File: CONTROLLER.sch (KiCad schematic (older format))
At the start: 75 parts, among them J23 Conn_02x03_Odd_Even, J24 ICSP, J25 Raspberry_Pi_2_3, Q13 DTC124E, Q14 DTC124E, Q15 DTC124E, Q16 DTC124E, Q17 DTC124E, Q18 BCX53, U11 CD4052B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

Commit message: RC2
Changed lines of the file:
@@
 U 1 1 5D6B516E
 P 9800 1875
-F 0 "C76" V 10025 1775 50  0000 L CNN
+F 0 "C76" V 10025 1800 50  0000 L CNN
 F 1 "100n" V 9950 1775 50  0000 L CNN
 F 2 "Capacitor_SMD:C_0805_2012Metric_Pad1.15x1.40mm_HandSolder" H 9838 1725 50  0001 C CNN
@@
 U 1 1 5F3CCF67
 P 13950 3925
-F 0 "C79" V 14100 3825 50  0000 L CNN
+F 0 "C79" V 14100 3850 50  0000 L CNN
 F 1 "100n" V 14175 3825 50  0000 L CNN
 F 2 "Capacitor_SMD:C_0805_2012Metric_Pad1.15x1.40mm_HandSolder" H 13988 3775 50  0001 C CNN
@@
 U 1 1 5DC83D54
 P 14200 7225
-F 0 "C81" V 14425 7175 50  0000 L CNN
+F 0 "C81" V 14425 7150 50  0000 L CNN
 F 1 "100n" V 14350 7125 50  0000 L CNN
 F 2 "Capacitor_SMD:C_0805_2012Metric_Pad1.15x1.40mm_HandSolder" H 14238 7075 50  0001 C CNN
@@
 U 1 1 5DC9523F
 P 14800 7725
-F 0 "C82" V 14650 7625 50  0000 L CNN
+F 0 "C82" V 14650 7650 50  0000 L CNN
 F 1 "100n" V 14575 7625 50  0000 L CNN
 F 2 "Capacitor_SMD:C_0805_2012Metric_Pad1.15x1.40mm_HandSolder" H 14838 7575 50  0001 C CNN
@@
 U 1 1 5F2AD05C
 P 3475 1000
-F 0 "C71" V 3250 950 50  0000 L CNN
+F 0 "C71" V 3250 925 50  0000 L CNN
 F 1 "100n" V 3325 900 50  0000 L CNN
 F 2 "Capacitor_SMD:C_0805_2012Metric_Pad1.15x1.40mm_HandSolder" H 3513 850 50  0001 C CNN
@@
 U 1 1 5F3D5069
 P 4475 1000
-F 0 "C72" V 4250 950 50  0000 L CNN
+F 0 "C72" V 4250 925 50  0000 L CNN
 F 1 "100n" V 4325 900 50  0000 L CNN
 F 2 "Capacitor_SMD:C_0805_2012Metric_Pad1.15x1.40mm_HandSolder" H 4513 850 50  0001 C CNN
@@
 U 1 1 5FFEA4EF
 P 14100 4575
-F 0 "C80" V 14300 4475 50  0000 L CNN
+F 0 "C80" V 14300 4500 50  0000 L CNN
 F 1 "100n" V 14225 4475 50  0000 L CNN
 F 2 "Capacitor_SMD:C_0805_2012Metric_Pad1.15x1.40mm_HandSolder" H 14138 4425 50  0001 C CNN
@@
 AR Path="/5CBD59C6/60291EF5" Ref="R94"  Part="1"
 F 0 "R94" V 1950 2175 50  0000 L CNN
-F 1 "1k" V 2025 2175 50  0000 L CNN
+F 1 "1k" V 2025 2200 50  0000 L CNN
 F 2 "Resistor_SMD:R_0805_2012Metric_Pad1.15x1.40mm_HandSolder" V 2055 2250 50  0001 C CNN
 F 3 "~" H 2125 2250 50  0001 C CNN
@@
 AR Path="/5E11E288/5FADAD98" Ref="R?"  Part="1"
 AR Path="/5CBD59C6/5FADAD98" Ref="R86"  Part="1"
-F 0 "R86" V 1850 5800 50  0000 R CNN
+F 0 "R86" V 1850 5775 50  0000 R CNN
 F 1 "10k" V 1775 5775 50  0000 R CNN
 F 2 "Resistor_SMD:R_0805_2012Metric_Pad1.15x1.40mm_HandSolder" V 1630 5700 50  0001 C CNN
@@
 AR Path="/5E11E288/5FB02049" Ref="C?"  Part="1"
 AR Path="/5CBD59C6/5FB02049" Ref="C65"  Part="1"
-F 0 "C65" V 2400 6425 50  0000 L CNN
-F 1 "10n" V 2325 6375 50  0000 L CNN
+F 0 "C65" V 2400 6400 50  0000 L CNN
+F 1 "10n" V 2325 6400 50  0000 L CNN
 F 2 "Capacitor_SMD:C_0805_2012Metric_Pad1.15x1.40mm_HandSolder" H 2238 6325 50  0001 C CNN
 F 3 "~" H 2200 6475 50  0001 C CNN
@@
 AR Path="/5E11E288/5FB52AE8" Ref="R?"  Part="1"
 AR Path="/5CBD59C6/5FB52AE8" Ref="R90"  Part="1"
-F 0 "R90" V 1775 6300 50  0000 R CNN
+F 0 "R90" V 1775 6325 50  0000 R CNN
 F 1 "10k" V 1850 6325 50  0000 R CNN
 F 2 "Resistor_SMD:R_0805_2012Metric_Pad1.15x1.40mm_HandSolder" V 1880 6250 50  0001 C CNN
@@
 AR Path="/5E11E288/5FC56E25" Ref="C?"  Part="1"
 AR Path="/5CBD59C6/5FC56E25" Ref="C60"  Part="1"
-F 0 "C60" V 1900 6425 50  0000 L CNN
-F 1 "1n" V 1825 6375 50  0000 L CNN
+F 0 "C60" V 1900 6400 50  0000 L CNN
+F 1 "1n" V 1825 6425 50  0000 L CNN
 F 2 "Capacitor_SMD:C_0805_2012Metric_Pad1.15x1.40mm_HandSolder" H 1738 6325 50  0001 C CNN
 F 3 "~" H 1700 6475 50  0001 C CNN
@@
 AR Path="/5E11E288/608C7882" Ref="R?"  Part="1"
 AR Path="/5CBD59C6/608C7882" Ref="R87"  Part="1"
-F 0 "R87" V 1850 7250 50  0000 R CNN
+F 0 "R87" V 1850 7225 50  0000 R CNN
 F 1 "10k" V 1775 7225 50  0000 R CNN
 F 2 "Resistor_SMD:R_0805_2012Metric_Pad1.15x1.40mm_HandSolder" V 1630 7150 50  0001 C CNN
@@
 AR Path="/5E11E288/608C7897" Ref="C?"  Part="1"
 AR Path="/5CBD59C6/608C7897" Ref="C66"  Part="1"
-F 0 "C66" V 2400 7875 50  0000 L CNN
+F 0 "C66" V 2400 7850 50  0000 L CNN
 F 1 "100n" V 2325 7825 50  0000 L CNN
 F 2 "Capacitor_SMD:C_0805_2012Metric_Pad1.15x1.40mm_HandSolder" H 2238 7775 50  0001 C CNN
@@
 AR Path="/5E11E288/608C78C8" Ref="C?"  Part="1"
 AR Path="/5CBD59C6/608C78C8" Ref="C61"  Part="1"
-F 0 "C61" V 1900 7875 50  0000 L CNN
-F 1 "1n" V 1825 7825 50  0000 L CNN
+F 0 "C61" V 1900 7850 50  0000 L CNN
+F 1 "1n" V 1825 7875 50  0000 L CNN
 F 2 "Capacitor_SMD:C_0805_2012Metric_Pad1.15x1.40mm_HandSolder" H 1738 7775 50  0001 C CNN
 F 3 "~" H 1700 7925 50  0001 C CNN
@@
 AR Path="/5E11E288/608F8D03" Ref="R?"  Part="1"
 AR Path="/5CBD59C6/608F8D03" Ref="R88"  Part="1"
-F 0 "R88" V 1850 8700 50  0000 R CNN
+F 0 "R88" V 1850 8675 50  0000 R CNN
 F 1 "10k" V 1775 8675 50  0000 R CNN
 F 2 "Resistor_SMD:R_0805_2012Metric_Pad1.15x1.40mm_HandSolder" V 1630 8600 50  0001 C CNN
@@
 AR Path="/5E11E288/608F8D18" Ref="C?"  Part="1"
 AR Path="/5CBD59C6/608F8D18" Ref="C67"  Part="1"
-F 0 "C67" V 2400 9325 50  0000 L CNN
+F 0 "C67" V 2400 9300 50  0000 L CNN
 F 1 "100n" V 2325 9275 50  0000 L CNN
 F 2 "Capacitor_SMD:C_0805_2012Metric_Pad1.15x1.40mm_HandSolder" H 2238 9225 50  0001 C CNN
@@
 AR Path="/5E11E288/608F8D2C" Ref="R?"  Part="1"
 AR Path="/5CBD59C6/608F8D2C" Ref="R92"  Part="1"
-F 0 "R92" V 1775 9200 50  0000 R CNN
+F 0 "R92" V 1775 9225 50  0000 R CNN
 F 1 "10k" V 1850 9225 50  0000 R CNN
 F 2 "Resistor_SMD:R_0805_2012Metric_Pad1.15x1.40mm_HandSolder" V 1880 9150 50  0001 C CNN
@@
 AR Path="/5E11E288/608F8D49" Ref="C?"  Part="1"
 AR Path="/5CBD59C6/608F8D49" Ref="C62"  Part="1"
-F 0 "C62" V 1900 9325 50  0000 L CNN
-F 1 "1n" V 1825 9275 50  0000 L CNN
+F 0 "C62" V 1900 9300 50  0000 L CNN
+F 1 "1n" V 1825 9325 50  0000 L CNN
 F 2 "Capacitor_SMD:C_0805_2012Metric_Pad1.15x1.40mm_HandSolder" H 1738 9225 50  0001 C CNN
 F 3 "~" H 1700 9375 50  0001 C CNN
@@
 AR Path="/5E11E288/608F8D8C" Ref="R?"  Part="1"
 AR Path="/5CBD59C6/608F8D8C" Ref="R89"  Part="1"
-F 0 "R89" V 1850 10150 50  0000 R CNN
+F 0 "R89" V 1850 10125 50  0000 R CNN
 F 1 "10k" V 1775 10125 50  0000 R CNN
 F 2 "Resistor_SMD:R_0805_2012Metric_Pad1.15x1.40mm_HandSolder" V 1630 10050 50  0001 C CNN
@@
 AR Path="/5E11E288/608F8DA1" Ref="C?"  Part="1"
 AR Path="/5CBD59C6/608F8DA1" Ref="C68"  Part="1"
-F 0 "C68" V 2400 10775 50  0000 L CNN
+F 0 "C68" V 2400 10750 50  0000 L CNN
 F 1 "100n" V 2325 10725 50  0000 L CNN
 F 2 "Capacitor_SMD:C_0805_2012Metric_Pad1.15x1.40mm_HandSolder" H 2238 10675 50  0001 C CNN
@@
 AR Path="/5E11E288/608F8DD2" Ref="C?"  Part="1"
 AR Path="/5CBD59C6/608F8DD2" Ref="C63"  Part="1"
-F 0 "C63" V 1900 10775 50  0000 L CNN
-F 1 "1n" V 1825 10725 50  0000 L CNN
+F 0 "C63" V 1900 10750 50  0000 L CNN
+F 1 "1n" V 1825 10775 50  0000 L CNN
 F 2 "Capacitor_SMD:C_0805_2012Metric_Pad1.15x1.40mm_HandSolder" H 1738 10675 50  0001 C CNN
 F 3 "~" H 1700 10825 50  0001 C CNN
@@
 AR Path="/5E11E288/5F2A2641" Ref="R?"  Part="1"
 AR Path="/5CBD59C6/5F2A2641" Ref="R99"  Part="1"
-F 0 "R99" V 7725 5450 50  0000 R CNN
+F 0 "R99" V 7725 5425 50  0000 R CNN
 F 1 "10k" V 7650 5425 50  0000 R CNN
 F 2 "Resistor_SMD:R_0805_2012Metric_Pad1.15x1.40mm_HandSolder" V 7505 5350 50  0001 C CNN
@@
 AR Path="/5E11E288/5F2A2637" Ref="R?"  Part="1"
 AR Path="/5CBD59C6/5F2A2637" Ref="R98"  Part="1"
-F 0 "R98" V 7475 5450 50  0000 R CNN
+F 0 "R98" V 7475 5425 50  0000 R CNN
 F 1 "10k" V 7400 5425 50  0000 R CNN
 F 2 "Resistor_SMD:R_0805_2012Metric_Pad1.15x1.40mm_HandSolder" V 7255 5350 50  0001 C CNN
@@
 P 2525 1875
 F 0 "C69" V 2325 1800 50  0000 L CNN
-F 1 "1n" V 2400 1775 50  0000 L CNN
+F 1 "1n" V 2400 1825 50  0000 L CNN
 F 2 "Capacitor_SMD:C_0805_2012Metric_Pad1.15x1.40mm_HandSolder" H 2563 1725 50  0001 C CNN
 F 3 "~" H 2525 1875 50  0001 C CNN
@@
 AR Path="/5E11E288/5F3EBDAF" Ref="R?"  Part="1"
 AR Path="/5CBD59C6/5F3EBDAF" Ref="R97"  Part="1"
-F 0 "R97" V 5625 8625 50  0000 R CNN
+F 0 "R97" V 5625 8600 50  0000 R CNN
 F 1 "4k7" V 5700 8600 50  0000 R CNN
 F 2 "Resistor_SMD:R_0805_2012Metric_Pad1.15x1.40mm_HandSolder" V 5730 8525 50  0001 C CNN
@@
 AR Path="/5E11E288/5F79A76B" Ref="C?"  Part="1"
 AR Path="/5CBD59C6/5F79A76B" Ref="C73"  Part="1"
-F 0 "C73" V 6425 9150 50  0000 L CNN
-F 1 "1n" V 6350 9100 50  0000 L CNN
+F 0 "C73" V 6425 9125 50  0000 L CNN
+F 1 "1n" V 6350 9150 50  0000 L CNN
 F 2 "Capacitor_SMD:C_0805_2012Metric_Pad1.15x1.40mm_HandSolder" H 6263 9050 50  0001 C CNN
 F 3 "~" H 6225 9200 50  0001 C CNN
@@
 AR Path="/5F2EB8E5" Ref="C?"  Part="1"
 AR Path="/5CBD59C6/5F2EB8E5" Ref="C78"  Part="1"
-F 0 "C78" V 13350 3875 50  0000 L CNN
+F 0 "C78" V 13350 3850 50  0000 L CNN
 F 1 "100n" V 13425 3825 50  0000 L CNN
 F 2 "Capacitor_SMD:C_0805_2012Metric_Pad1.15x1.40mm_HandSolder" H 13588 3775 50  0001 C CNN

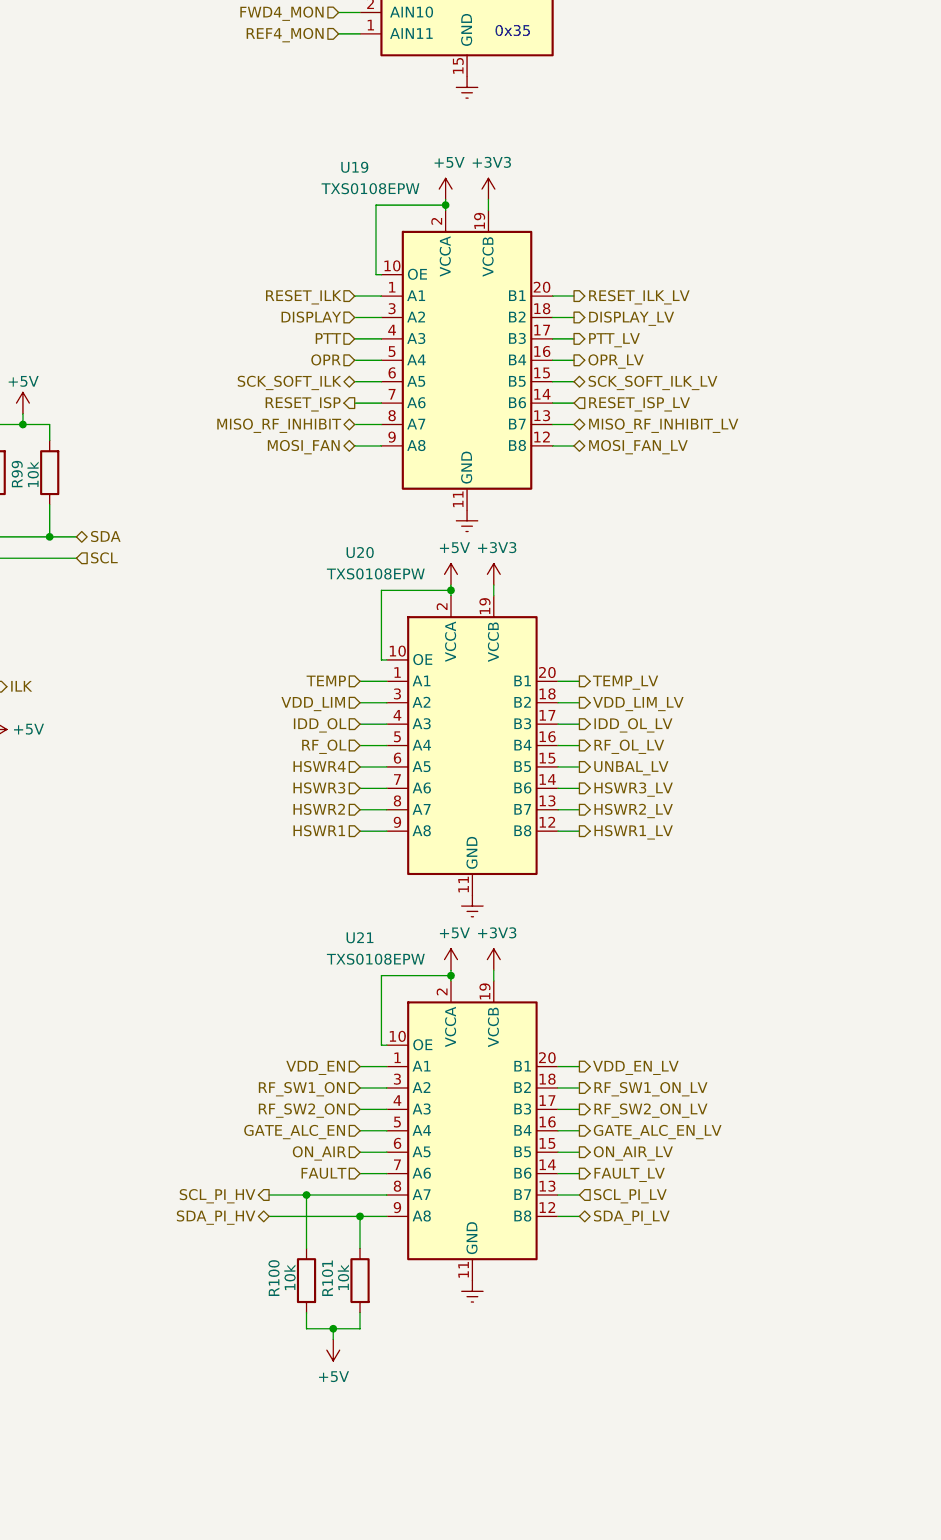
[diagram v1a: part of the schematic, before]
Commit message: bug fix level shifter U19-U21 VCCA VCCB swap
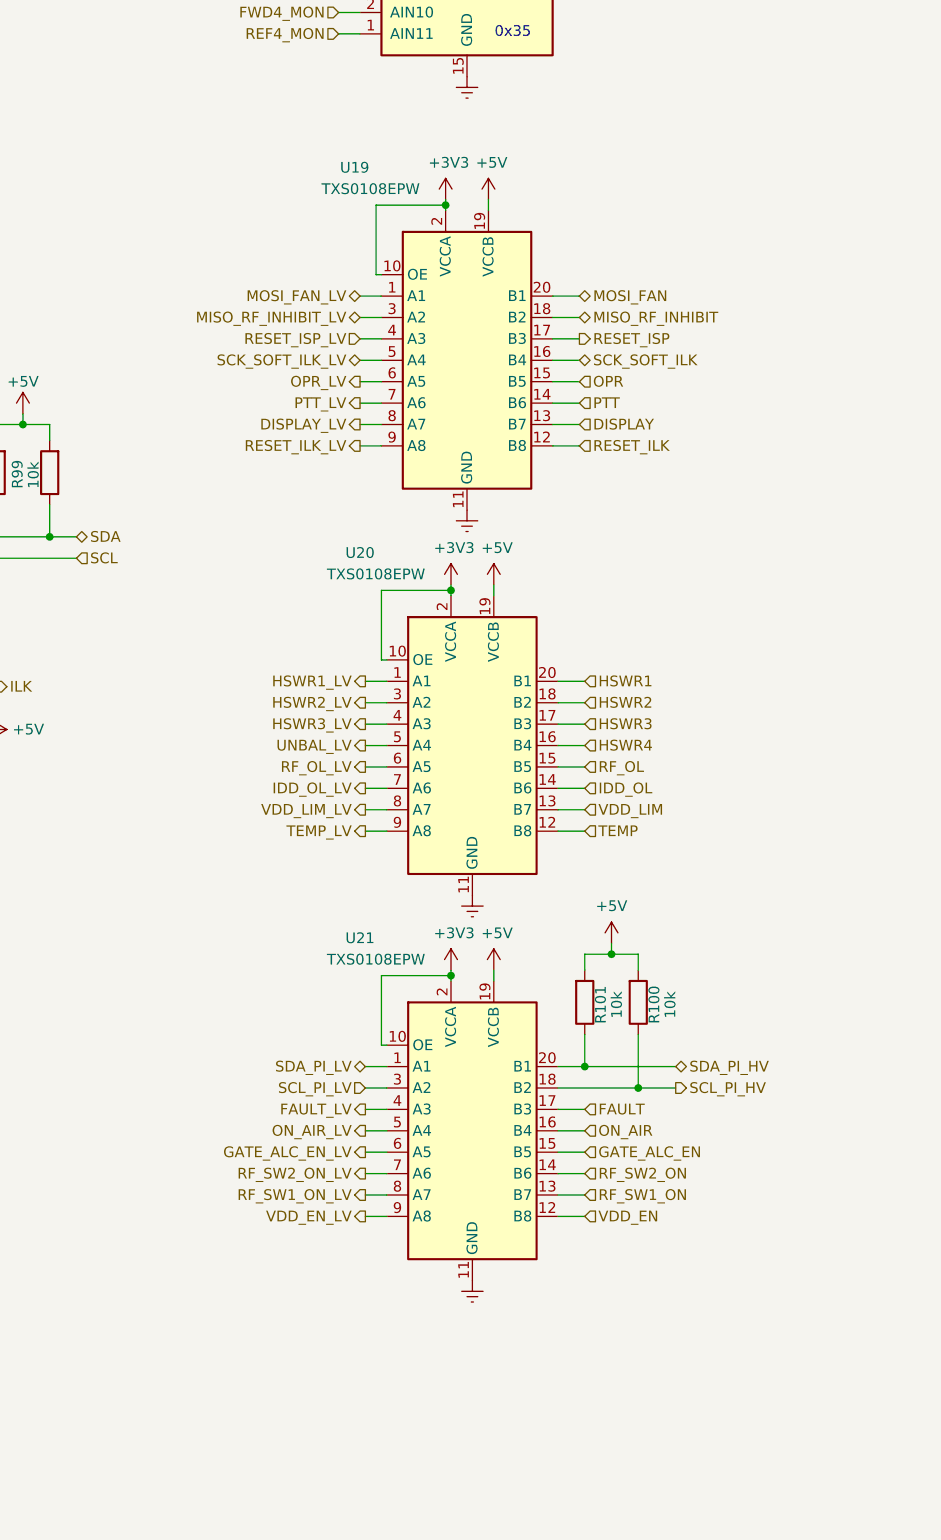
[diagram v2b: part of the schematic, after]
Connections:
- net +3V3: now also U19.10 (OE), U19.2 (VCCA), U20.10 (OE), U20.2 (VCCA), U21.10 (OE), U21.2 (VCCA); no longer U19.19 (VCCB), U20.19 (VCCB), U21.19 (VCCB)
- net +5V: now also U19.19 (VCCB), U20.19 (VCCB), U21.19 (VCCB); no longer U19.10 (OE), U19.2 (VCCA), U20.10 (OE), U20.2 (VCCA), U21.10 (OE), U21.2 (VCCA)
- net DISPLAY: now also U19.13 (B7); no longer U19.3 (A2)
- net DISPLAY_LV: now also U19.8 (A7); no longer U19.18 (B2)
- net FAULT: now also U21.17 (B3); no longer U21.7 (A6)
- net FAULT_LV: now also U21.4 (A3); no longer U21.14 (B6)
- net GATE_ALC_EN: now also U21.15 (B5); no longer U21.5 (A4)
- net GATE_ALC_EN_LV: now also U21.6 (A5); no longer U21.16 (B4)
- net HSWR1: now also U20.20 (B1); no longer U20.9 (A8)
- net HSWR1_LV: now also U20.1 (A1); no longer U20.12 (B8)
- net HSWR2: now also U20.18 (B2); no longer U20.8 (A7)
- net HSWR2_LV: now also U20.3 (A2); no longer U20.13 (B7)
- net HSWR3: now also U20.17 (B3); no longer U20.7 (A6)
- net HSWR3_LV: now also U20.4 (A3); no longer U20.14 (B6)
- net HSWR4: now also U20.16 (B4); no longer U20.6 (A5)
- net IDD_OL: now also U20.14 (B6); no longer U20.4 (A3)
- net IDD_OL_LV: now also U20.7 (A6); no longer U20.17 (B3)
- net MISO_RF_INHIBIT: now also U19.18 (B2); no longer U19.8 (A7)
- net MISO_RF_INHIBIT_LV: now also U19.3 (A2); no longer U19.13 (B7)
- net MOSI_FAN: now also U19.20 (B1); no longer U19.9 (A8)
- net MOSI_FAN_LV: now also U19.1 (A1); no longer U19.12 (B8)
- net ON_AIR: now also U21.16 (B4); no longer U21.6 (A5)
- net ON_AIR_LV: now also U21.5 (A4); no longer U21.15 (B5)
- net OPR: now also U19.15 (B5); no longer U19.5 (A4)
- net OPR_LV: now also U19.6 (A5); no longer U19.16 (B4)
- net PTT: now also U19.14 (B6); no longer U19.4 (A3)
- net PTT_LV: now also U19.7 (A6); no longer U19.17 (B3)
- net RESET_ILK: now also U19.12 (B8); no longer U19.1 (A1)
- net RESET_ILK_LV: now also U19.9 (A8); no longer U19.20 (B1)
- net RESET_ISP: now also U19.17 (B3); no longer U19.7 (A6)
- net RESET_ISP_LV: now also U19.4 (A3); no longer U19.14 (B6)
- net RF_OL: now also U20.15 (B5); no longer U20.5 (A4)
- net RF_OL_LV: now also U20.6 (A5); no longer U20.16 (B4)
- net RF_SW1_ON: now also U21.13 (B7); no longer U21.3 (A2)
- net RF_SW1_ON_LV: now also U21.8 (A7); no longer U21.18 (B2)
- net RF_SW2_ON: now also U21.14 (B6); no longer U21.4 (A3)
- net RF_SW2_ON_LV: now also U21.7 (A6); no longer U21.17 (B3)
- net SCK_SOFT_ILK: now also U19.16 (B4); no longer U19.6 (A5)
- net SCK_SOFT_ILK_LV: now also U19.5 (A4); no longer U19.15 (B5)
- net SCL_PI_HV: now also U21.18 (B2); no longer U21.8 (A7)
- net SCL_PI_LV: now also U21.3 (A2); no longer U21.13 (B7)
- net SDA_PI_HV: now also U21.20 (B1); no longer U21.9 (A8)
- net SDA_PI_LV: now also U21.1 (A1); no longer U21.12 (B8)
- net TEMP: now also U20.12 (B8); no longer U20.1 (A1)
- net TEMP_LV: now also U20.9 (A8); no longer U20.20 (B1)
- net UNBAL_LV: now also U20.5 (A4); no longer U20.15 (B5)
- net VDD_EN: now also U21.12 (B8); no longer U21.1 (A1)
- net VDD_EN_LV: now also U21.9 (A8); no longer U21.20 (B1)
- net VDD_LIM: now also U20.13 (B7); no longer U20.3 (A2)
- net VDD_LIM_LV: now also U20.8 (A7); no longer U20.18 (B2)
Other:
- moved on the sheet: R100, R101
